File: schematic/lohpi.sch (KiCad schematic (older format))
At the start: 0 parts

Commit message: Updates to schematic, components
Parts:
- added J? (x4): CONN_01X01, symbol CONN_01X01
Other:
- note added: "Mounting Holes"
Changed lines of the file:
@@
 Wire Wire Line
 	3500 5400 4600 5400
+$Comp
+L CONN_01X01 J?
+U 1 1 59B4EB9A
+P 1750 6600
+F 0 "J?" H 1828 6641 50  0000 L CNN
+F 1 "CONN_01X01" H 1828 6550 50  0000 L CNN
+F 2 "" H 1750 6600 50  0001 C CNN
+F 3 "" H 1750 6600 50  0001 C CNN
+	1    1750 6600
+	1    0    0    -1
+$EndComp
+$Comp
+L CONN_01X01 J?
+U 1 1 59B4F0CE
+P 1750 6800
+F 0 "J?" H 1828 6841 50  0000 L CNN
+F 1 "CONN_01X01" H 1828 6750 50  0000 L CNN
+F 2 "" H 1750 6800 50  0001 C CNN
+F 3 "" H 1750 6800 50  0001 C CNN
+	1    1750 6800
+	1    0    0    -1
+$EndComp
+$Comp
+L CONN_01X01 J?
+U 1 1 59B4F26C
+P 1750 7000
+F 0 "J?" H 1828 7041 50  0000 L CNN
+F 1 "CONN_01X01" H 1828 6950 50  0000 L CNN
+F 2 "" H 1750 7000 50  0001 C CNN
+F 3 "" H 1750 7000 50  0001 C CNN
+	1    1750 7000
+	1    0    0    -1
+$EndComp
+$Comp
+L CONN_01X01 J?
+U 1 1 59B4F40C
+P 1750 7200
+F 0 "J?" H 1828 7241 50  0000 L CNN
+F 1 "CONN_01X01" H 1828 7150 50  0000 L CNN
+F 2 "" H 1750 7200 50  0001 C CNN
+F 3 "" H 1750 7200 50  0001 C CNN
+	1    1750 7200
+	1    0    0    -1
+$EndComp
+Text Notes 1500 6500 0    60   ~ 0
+Mounting Holes
 $EndSCHEMATC

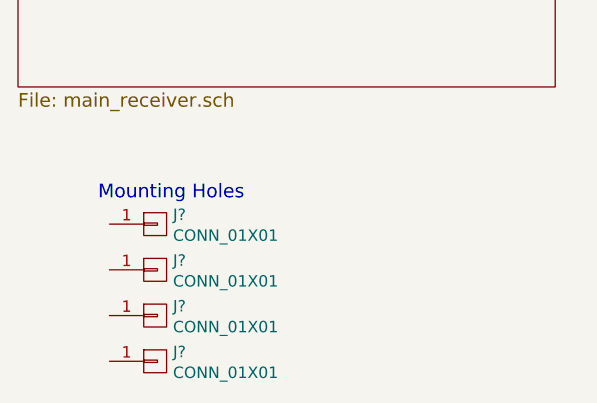
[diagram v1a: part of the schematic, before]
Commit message: Schematic capture almost done. RF layout started.
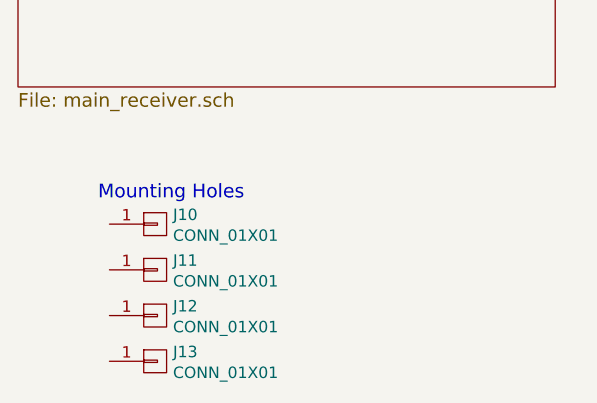
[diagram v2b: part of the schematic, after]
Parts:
- J10, J11, J12, J13: renamed from J?; footprint (none) -> rpi_mounting_hole:rpi_mounting_hole
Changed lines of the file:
@@
-EESchema Schematic File Version 2
+EESchema Schematic File Version 3
 LIBS:lohpi-rescue
 LIBS:power
@@
 LIBS:digital-audio
 LIBS:philips
-LIBS:display
 LIBS:cypress
 LIBS:siliconi
@@
 	3500 5400 4600 5400
 $Comp
-L CONN_01X01 J?
+L CONN_01X01 J10
 U 1 1 59B4EB9A
 P 1750 6600
-F 0 "J?" H 1828 6641 50  0000 L CNN
+F 0 "J10" H 1828 6641 50  0000 L CNN
 F 1 "CONN_01X01" H 1828 6550 50  0000 L CNN
-F 2 "" H 1750 6600 50  0001 C CNN
+F 2 "rpi_mounting_hole:rpi_mounting_hole" H 1750 6600 50  0001 C CNN
 F 3 "" H 1750 6600 50  0001 C CNN
 	1    1750 6600
@@
 $EndComp
 $Comp
-L CONN_01X01 J?
+L CONN_01X01 J11
 U 1 1 59B4F0CE
 P 1750 6800
-F 0 "J?" H 1828 6841 50  0000 L CNN
+F 0 "J11" H 1828 6841 50  0000 L CNN
 F 1 "CONN_01X01" H 1828 6750 50  0000 L CNN
-F 2 "" H 1750 6800 50  0001 C CNN
+F 2 "rpi_mounting_hole:rpi_mounting_hole" H 1750 6800 50  0001 C CNN
 F 3 "" H 1750 6800 50  0001 C CNN
 	1    1750 6800
@@
 $EndComp
 $Comp
-L CONN_01X01 J?
+L CONN_01X01 J12
 U 1 1 59B4F26C
 P 1750 7000
-F 0 "J?" H 1828 7041 50  0000 L CNN
+F 0 "J12" H 1828 7041 50  0000 L CNN
 F 1 "CONN_01X01" H 1828 6950 50  0000 L CNN
-F 2 "" H 1750 7000 50  0001 C CNN
+F 2 "rpi_mounting_hole:rpi_mounting_hole" H 1750 7000 50  0001 C CNN
 F 3 "" H 1750 7000 50  0001 C CNN
 	1    1750 7000
@@
 $EndComp
 $Comp
-L CONN_01X01 J?
+L CONN_01X01 J13
 U 1 1 59B4F40C
 P 1750 7200
-F 0 "J?" H 1828 7241 50  0000 L CNN
+F 0 "J13" H 1828 7241 50  0000 L CNN
 F 1 "CONN_01X01" H 1828 7150 50  0000 L CNN
-F 2 "" H 1750 7200 50  0001 C CNN
+F 2 "rpi_mounting_hole:rpi_mounting_hole" H 1750 7200 50  0001 C CNN
 F 3 "" H 1750 7200 50  0001 C CNN
 	1    1750 7200

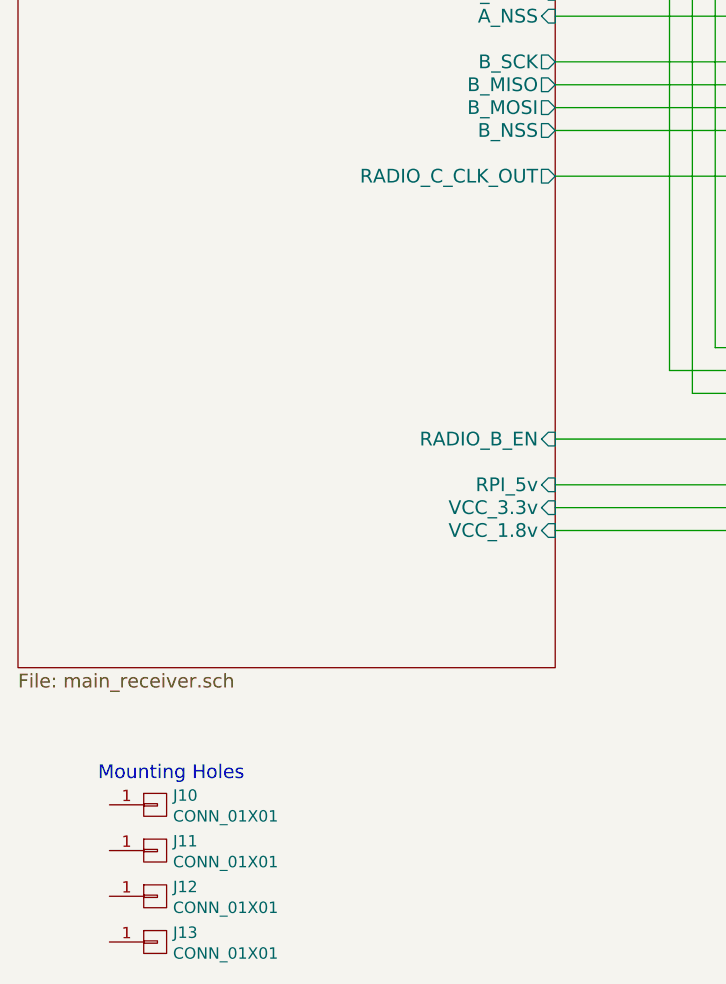
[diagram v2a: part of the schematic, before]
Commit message: RF layout updated. Rest still needs work
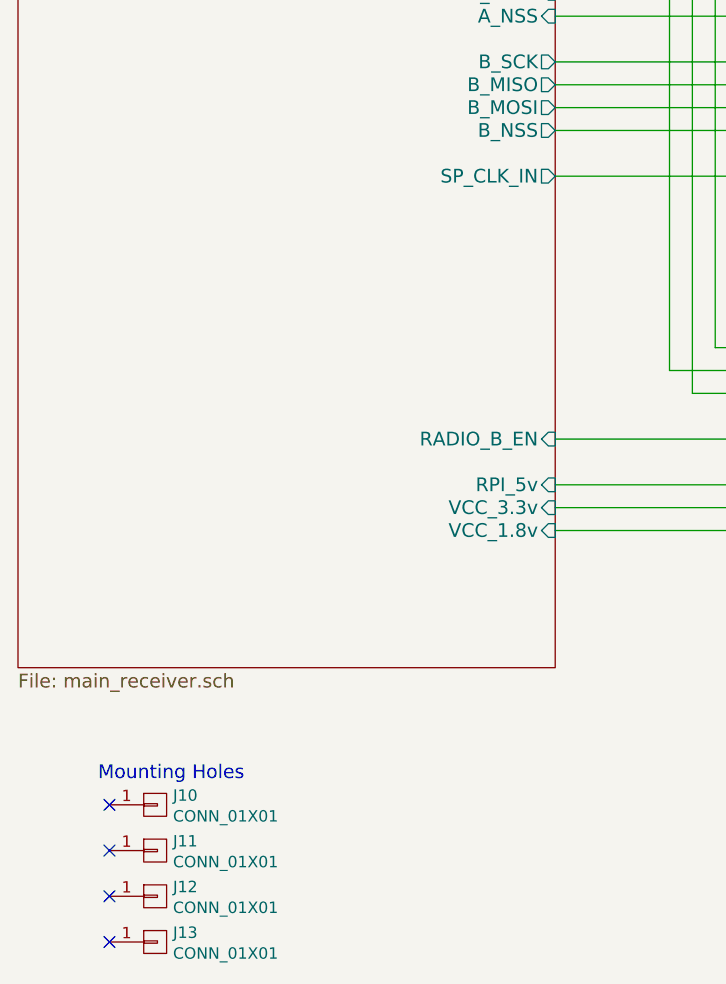
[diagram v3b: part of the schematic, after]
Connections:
- no-connect marks 0 -> 4
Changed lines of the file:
@@
 LIBS:digital-audio
 LIBS:philips
+LIBS:display
 LIBS:cypress
 LIBS:siliconi
@@
 F24 "B_MISO" O R 3500 3450 60
 F25 "B_SCK" O R 3500 3350 60
-F26 "RADIO_C_CLK_OUT" O R 3500 3850 60
-F27 "VCC_3.3v" I R 3500 5300 60
-F28 "VCC_1.8v" I R 3500 5400 60
+F26 "VCC_3.3v" I R 3500 5300 60
+F27 "VCC_1.8v" I R 3500 5400 60
+F28 "SP_CLK_IN" O R 3500 3850 60
 $EndSheet
 $Sheet
@@
 Text Notes 1500 6500 0    60   ~ 0
 Mounting Holes
+NoConn ~ 1550 6600
+NoConn ~ 1550 6800
+NoConn ~ 1550 7000
+NoConn ~ 1550 7200
 $EndSCHEMATC
